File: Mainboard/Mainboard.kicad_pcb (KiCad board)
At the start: 2 copper layers, 75 x 50 mm, 20 parts, among them J1 Conn_01x05, J2 Conn_02x08_Odd_Even, J3 Conn_02x06_Odd_Even, J4 Conn_02x06_Odd_Even, J5 Conn_02x02_Odd_Even, U1 ESP32-WROOM-32D, U2 ATxmega128A4U-AU

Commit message: Initial commit2
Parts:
- added D1: D, Diode_SMD:D_0603_1608Metric, F.Cu at (159.4, 81.9)
- added D2: D, Diode_SMD:D_0603_1608Metric, F.Cu at (159.4, 84.5)
- added H1: MountingHole_Pad, MountingHole:MountingHole_2.2mm_M2_DIN965_Pad, F.Cu at (144.9, 83.7)
- added H2: MountingHole_Pad, MountingHole:MountingHole_2.2mm_M2_DIN965_Pad, F.Cu at (151.4, 77.9)
- added H3: MountingHole_Pad, MountingHole:MountingHole_2.2mm_M2_DIN965_Pad, F.Cu at (150.2, 83.7)
- added H4: MountingHole_Pad, MountingHole:MountingHole_2.2mm_M2_DIN965_Pad, F.Cu at (156.7, 77.9)
- added Q1: BSS123, Package_TO_SOT_SMD:SOT-23, F.Cu at (145.4, 77.5)
- added Q2: AO3401A, Package_TO_SOT_SMD:SOT-23, F.Cu at (155.1, 82.9)
- added R7: 100K, Resistor_SMD:R_0402_1005Metric, F.Cu at (160.9, 76.3)
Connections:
- net GND renamed -BATT

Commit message: power management
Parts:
- removed H1, H2, H3, H4: MountingHole_Pad, MountingHole:MountingHole_2.2mm_M2_DIN965_Pad
- added C7: 1u, Capacitor_SMD:C_0402_1005Metric, F.Cu at (148.1, 64.8)
- added C8: 2.2u, Capacitor_SMD:C_0402_1005Metric, F.Cu at (148.1, 59.1)
- added C9: C, Capacitor_SMD:C_0402_1005Metric, F.Cu at (163.8, 45.7)
- added J6: Conn_01x04, Connector_PinHeader_2.54mm:PinHeader_1x04_P2.54mm_Vertical, F.Cu at (158.8, 80.0)
- added J7: Conn_01x02, Connector_PinHeader_2.54mm:PinHeader_1x02_P2.54mm_Vertical, F.Cu at (139.1, 69.2)
- added J8: Conn_01x02, Connector_PinHeader_2.54mm:PinHeader_1x02_P2.54mm_Vertical, F.Cu at (151.1, 80.0)
- added J9: Conn_01x04, Connector_PinHeader_2.54mm:PinHeader_1x04_P2.54mm_Vertical, F.Cu at (151.1, 67.3)
- added R10: 1.5K, Resistor_SMD:R_0402_1005Metric, F.Cu at (128.9, 70.5)
- added R11: 0.27, Resistor_SMD:R_1206_3216Metric, F.Cu at (135.3, 70.2)
- added R8: 33K, Resistor_SMD:R_0402_1005Metric, F.Cu at (146.1, 59.8)
- added R9: 33K, Resistor_SMD:R_0402_1005Metric, F.Cu at (146.1, 54.1)
- added U3: LN1152, Package_TO_SOT_SMD:SOT-23-5, F.Cu at (148.6, 62.4)
- added U4: TP4059, Package_TO_SOT_SMD:SOT-23-6, F.Cu at (132.1, 70.5)
- moved R7 18.0 mm to (143.5, 71.6), turned to 90 degrees
- moved Q2 13.4 mm to (148.3, 71.4), turned to 90 degrees
- moved D1 11.5 mm to (149.4, 76.2), turned to 180 degrees
- moved D2 10.5 mm to (152.9, 76.2)
- moved J4 3.81 mm to (174.0, 67.3)
- moved R6 3.81 mm to (170.3, 67.3)
- moved J2 2.54 mm to (115.1, 53.3)
- moved Q1 1.32 mm to (145.1, 76.2)
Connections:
- D2 pad 2: (no net) -> /PWRBTN_IN
- Q1 pad 1: (no net) -> /KEEPALIVE
- Q2 pad 2: VCC -> +VSW
- U2 pad 1: (no net) -> /BATT_MEAS
- U2 pad 23: (no net) -> /KEEPALIVE
- U2 pad 24: (no net) -> /PWRBTN_IN
- U2 pad 25: (no net) -> /BATT_NCHRG
- U2 pad 26: (no net) -> /USB_D-
- U2 pad 27: (no net) -> /USB_D+
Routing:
- net /BATT_NCHRG: track 0.00 -> 33.3 mm, vias 0 -> 2
- net Net-(J6-Pad1): track 0.00 -> 32.5 mm
- net /BATT_MEAS: track 0.00 -> 31.1 mm, vias 0 -> 2
- net /KEEPALIVE: track 0.00 -> 29.2 mm, vias 0 -> 3
- net /USB_D+: track 0.00 -> 25.8 mm, vias 0 -> 1
- net /USB_D-: track 0.00 -> 25.4 mm, vias 0 -> 1
- net /PWRBTN_IN: track 0.00 -> 18.8 mm, vias 0 -> 2
- net +BATT: track 0.00 -> 17.1 mm
- net +VSW: track 0.00 -> 15.5 mm
- net Net-(D1-Pad2): track 0.00 -> 10.3 mm
- net Net-(D1-Pad1): track 0.00 -> 5.81 mm
- net -BATT: track 27.7 -> 33.4 mm, vias 7 -> 41
- net /RCON_X: track 32.1 -> 28.3 mm
- net /RCON_Y: track 34.0 -> 30.2 mm
- net /RCON_AUD: track 97.4 -> 93.6 mm
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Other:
- board size 75 x 50 mm -> 70 x 45.1 mm
- net class Power added: clearance 0.2, trace_width 0.5, via_dia 0.8, via_drill 0.4

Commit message: finetuning
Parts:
- added C10: 10u, Capacitor_SMD:C_0603_1608Metric, F.Cu at (141.6, 70.5)
- added C11: 100n, Capacitor_SMD:C_0402_1005Metric, F.Cu at (171.0, 72.4)
- added C12: 100n, Capacitor_SMD:C_0402_1005Metric, F.Cu at (171.0, 69.8)
- added C13: 100n, Capacitor_SMD:C_0402_1005Metric, F.Cu at (170.8, 51.0)
- added C14: 100n, Capacitor_SMD:C_0402_1005Metric, F.Cu at (167.0, 47.8)
- C9: value C -> 100n
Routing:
- net -BATT: track 33.4 -> 40.1 mm, vias 41 -> 42
- net /RCON_Y: track 30.2 -> 28.7 mm
- net /RCON_X: track 28.3 -> 27.2 mm
- net /LCON_Y: track 12.8 -> 13.8 mm
- net /LCON_X: track 12.1 -> 12.6 mm
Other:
- board text added: "5V"
- board text added: "BAT+"
- board text added: "BAT-"
- board text added: "D+"
- board text added: "D-"
- board text added: "H-HTV-Matrix"
- board text added: "LCON"
- board text added: "PWRBTN"
- board text added: "RCON"
- board text added: "VCC"

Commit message: fixing
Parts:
- added C15: 10u, Capacitor_SMD:C_0603_1608Metric, F.Cu at (137.3, 74.3)
- added C16: 22u, Capacitor_SMD:C_1206_3216Metric, F.Cu at (146.9, 70.5)
- added C17: 10u, Capacitor_SMD:C_0402_1005Metric, F.Cu at (121.9, 47.6)
- C11, C12, C13, C14, C9: value 100n -> 100p
- R11: footprint Resistor_SMD:R_1206_3216Metric -> Resistor_SMD:R_0805_2012Metric
- U4: value TP4059 -> TP4056; footprint Package_TO_SOT_SMD:SOT-23-6 -> Package_SO:HSOP-8-1EP_3.9x4.9mm_P1.27mm_EP2.41x3.1mm_ThermalVias
- moved R2 9.69 mm to (153.5, 42.5), turned to 180 degrees
- moved R11 6.30 mm to (134.6, 76.5)
- moved R10 5.74 mm to (131.6, 75.6), turned to 180 degrees
- moved R7 2.50 mm to (144.8, 73.8)
- moved Q2 1.91 mm to (148.3, 73.3)
- moved Q1 1.27 mm to (143.8, 76.2)
- moved U4 0.90 mm to (132.7, 71.1)
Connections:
- Q2 pad 2: +VSW -> +BATT
- Q2 pad 3: +BATT -> +VSW
- R10 pad 1: -BATT -> Net-(R10-Pad1)
- R10 pad 2: Net-(R10-Pad2) -> -BATT
- U4 pad 1: /BATT_NCHRG -> -BATT
- U4 pad 2: -BATT -> Net-(R10-Pad1)
- U4 pad 3: +BATT -> -BATT
- U4 pad 5: /BATT_NCHRG -> +BATT
- U4 pad 6: Net-(R10-Pad2) -> /BATT_NCHRG
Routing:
- net /USB_VCC: track 2.26 -> 18.6 mm
- net /LCON_BM_A: track 65.4 -> 52.8 mm
- net -BATT: track 40.1 -> 46.9 mm, vias 42 -> 43
- net Net-(J6-Pad1): track 32.5 -> 27.0 mm
- net VCC: track 111.9 -> 117.3 mm, vias 2 -> 4
- net Net-(D1-Pad2): track 10.3 -> 5.72 mm
- net /LCON_BM_B: track 63.4 -> 59.7 mm, vias 2 -> 3
- net /RCON_Y: track 28.7 -> 31.2 mm
- net /RCON_X: track 27.2 -> 29.8 mm
- net Net-(R10-Pad2): track 2.47 -> 0.00 mm
- net Net-(R10-Pad1): track 0.00 -> 1.80 mm
- net /ATX_SCK: track 13.5 -> 11.8 mm
- net /LCON_BM_C: track 62.5 -> 60.9 mm
- net /KEEPALIVE: track 29.2 -> 30.5 mm
- net +VSW: track 15.5 -> 16.6 mm
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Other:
- board text added: "by Lars"

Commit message: Mainboard finished?
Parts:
- C8: value 2.2u -> 10u; footprint Capacitor_SMD:C_0402_1005Metric -> Capacitor_SMD:C_0805_2012Metric
- moved R8 2.92 mm to (146.1, 56.9)
- moved C9 1.30 mm to (165.1, 45.7)
- moved R9 1.13 mm to (145.5, 53.1), turned to 0 degrees
- moved C15 1.10 mm to (136.5, 73.5), turned to 90 degrees
- moved C4 0.89 mm to (150.1, 53.1)
- moved C8 0.56 mm to (148.7, 58.9)
- moved Q1 0.51 mm to (143.8, 76.7)
- moved C1 0.45 mm to (122.5, 43.0)
- moved C3 0.35 mm to (159.5, 59.2)
- moved C10 0.14 mm to (141.6, 70.6)
- moved Q2 0.09 mm to (148.3, 73.4)
- moved R11 0.08 mm to (134.6, 76.6)
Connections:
- U2 pad 20: /LCON_BM_A -> /LCON_BM_C
- U2 pad 22: /LCON_BM_C -> /LCON_BM_A
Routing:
- net VCC: track 117.3 -> 128.6 mm, vias 4 -> 8
- net /LCON_BM_A: track 52.8 -> 61.5 mm, vias 2 -> 1
- net /LCON_BM_C: track 60.9 -> 67.3 mm, vias 1 -> 0
- net /LCON_BM_B: track 59.7 -> 64.7 mm, vias 3 -> 0
- net /PDI_CLK: track 12.3 -> 7.49 mm
- net /ATX_MOSI: track 13.6 -> 10.3 mm
- net +VSW: track 16.6 -> 19.5 mm
- net Net-(D1-Pad2): track 5.72 -> 8.55 mm
- net /KEEPALIVE: track 30.5 -> 32.7 mm
- net /RCON_BM_2: track 31.5 -> 29.7 mm
- net /BATT_NCHRG: track 33.6 -> 32.3 mm
- net /BATT_MEAS: track 31.1 -> 30.0 mm
- net /PDI_DATA: track 4.84 -> 5.87 mm, vias 1 -> 0
- net /ATX_SCK: track 11.8 -> 12.7 mm
- net /PWRBTN_IN: track 18.8 -> 19.7 mm
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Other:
- board text added: "A"
- board text added: "B"
- board text added: "B1"
- board text added: "B2"
- board text added: "C"
- board text added: "CLK"
- board text added: "D"
- board text added: "E"
- board text added: "G1"
- board text added: "G2"
- board text added: "LAT"
- board text added: "OE"
- board text added: "R1"
- board text added: "R2"
- board text added: "Rev A"

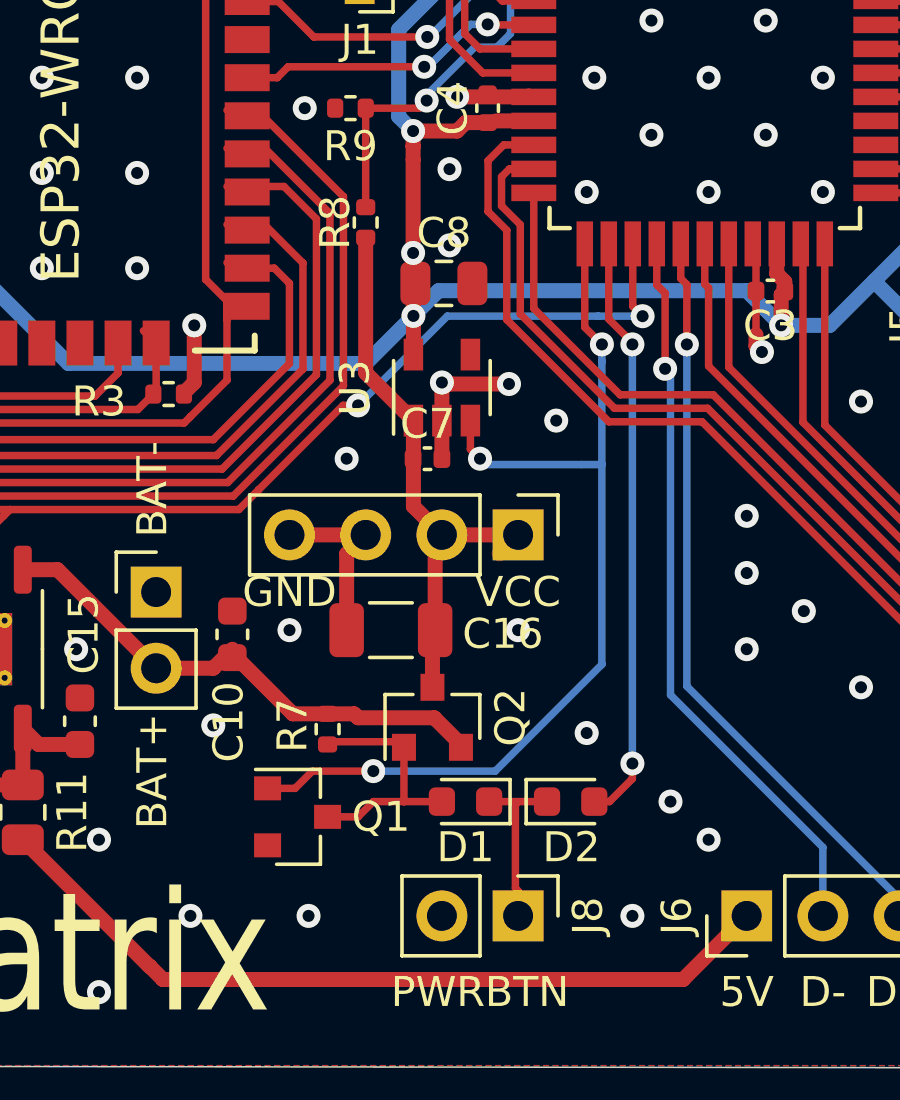
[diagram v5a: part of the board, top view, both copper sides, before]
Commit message: more powerfull main pfet
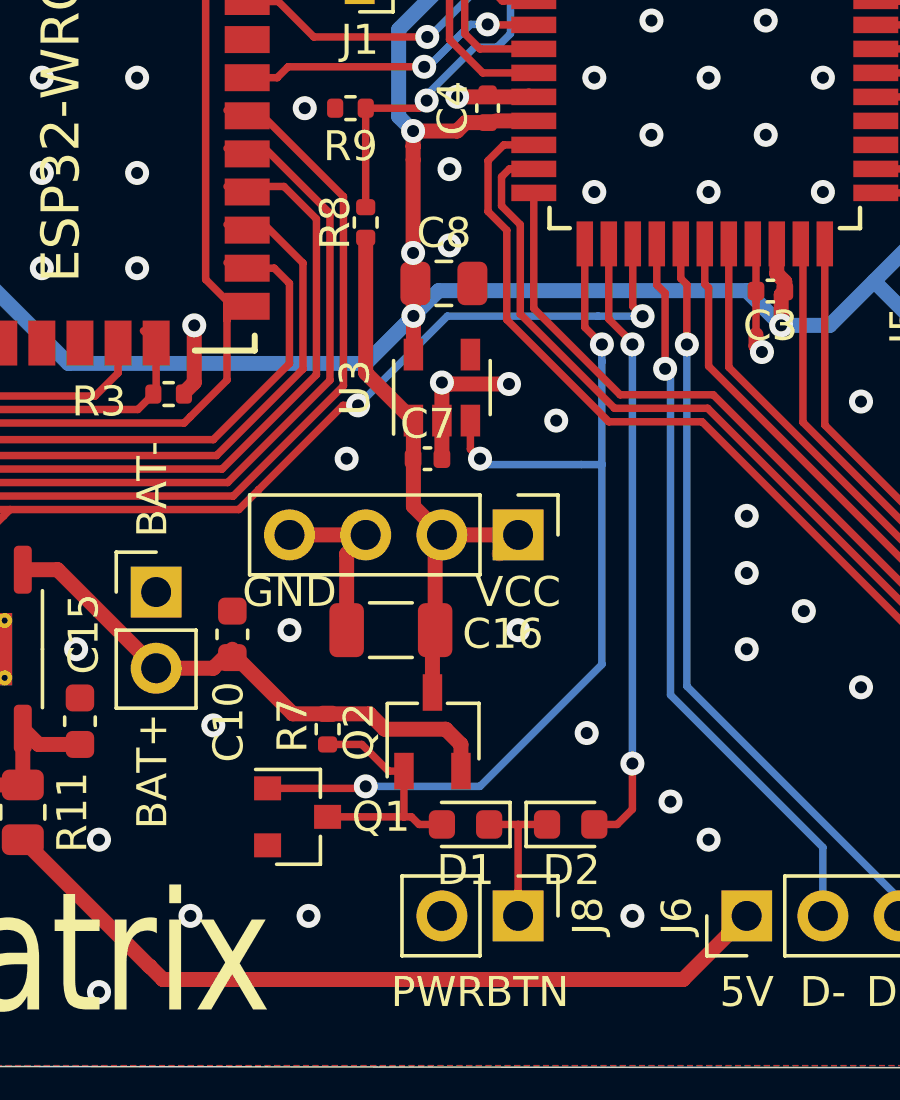
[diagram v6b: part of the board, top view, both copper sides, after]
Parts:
- Q2: value AO3401A -> WST3415; footprint Package_TO_SOT_SMD:SOT-23 -> Package_TO_SOT_SMD:TSOT-23
- moved D1 0.76 mm to (149.4, 77.0)
- moved D2 0.76 mm to (152.9, 77.0)
- moved Q2 0.48 mm to (148.3, 73.9)
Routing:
- net /PWRBTN_IN: track 19.7 -> 20.7 mm
- net +BATT: track 17.6 -> 18.4 mm
